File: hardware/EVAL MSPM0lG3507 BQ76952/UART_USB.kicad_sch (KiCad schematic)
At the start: 14 parts, among them J16 USB_B_Micro, Q1 2N7002, U1 ISO7721D, U12 FT230XS, U4 ISO7721D, U8 TPD4E05U06DQA

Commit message: boards finalized
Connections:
- net GND: now also J16.5 (GND), Q1.3 (D); no longer C8.2, C9.2, Q1.2 (S), U1.4 (GND1), U12.13 (GND), U12.5 (GND), U4.4 (GND1)
- new net: C8.2, C9.2, Q1.2 (S), U1.4 (GND1), U12.13 (GND), U12.5 (GND), U4.4 (GND1)
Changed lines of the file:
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@@
+	(wire
+		(pts
+			(xy 148.59 115.57) (xy 148.59 93.98)
+		)
+		(stroke
+			(width 0)
+			(type default)
+		)
+	)
+	(wire
+		(pts
+			(xy 151.13 86.36) (xy 153.67 86.36)
+		)
+		(stroke
+			(width 0)
+			(type default)
+		)
+	)
+	(wire
+		(pts
+			(xy 115.57 120.65) (xy 115.57 123.19)
+		)
+		(stroke
+			(width 0)
+			(type default)
+		)
+	)
+	(wire
+		(pts
+			(xy 143.51 91.44) (xy 143.51 95.25)
+		)
+		(stroke
+			(width 0)
+			(type default)
+		)
+	)
+	(wire
+		(pts
+			(xy 63.5 102.87) (xy 58.42 102.87)
+		)
+		(stroke
+			(width 0)
+			(type default)
+		)
+	)
+	(wire
+		(pts
+			(xy 50.8 110.49) (xy 50.8 123.19)
+		)
+		(stroke
+			(width 0)
+			(type default)
+		)
+	)
+	(wire
+		(pts
+			(xy 184.15 115.57) (xy 191.77 115.57)
+		)
+		(stroke
+			(width 0)
+			(type default)
+		)
+	)
+	(wire
+		(pts
+			(xy 58.42 100.33) (xy 64.77 100.33)
+		)
+		(stroke
+			(width 0)
+			(type default)
+		)
+	)
+	(wire
+		(pts
+			(xy 135.89 95.25) (xy 143.51 95.25)
+		)
+		(stroke
+			(width 0)
+			(type default)
+		)
+	)
+	(wire
+		(pts
+			(xy 140.97 88.9) (xy 153.67 88.9)
+		)
+		(stroke
+			(width 0)
+			(type default)
+		)
+	)
+	(wire
+		(pts
+			(xy 151.13 107.95) (xy 151.13 86.36)
+		)
+		(stroke
+			(width 0)
+			(type default)
+		)
+	)
+	(polyline
+		(pts
+			(xy 131.572 118.11) (xy 131.572 119.126)
+		)
+		(stroke
+			(width 0)
+			(type default)
+			(color 218 0 255 1)
+		)
+	)
+	(wire
+		(pts
+			(xy 120.65 81.28) (xy 88.9 81.28)
+		)
+		(stroke
+			(width 0)
+			(type default)
+		)
+	)
+	(wire
+		(pts
+			(xy 92.71 92.71) (xy 100.33 92.71)
+		)
+		(stroke
+			(width 0)
+			(type default)
+		)
+	)
+	(wire
+		(pts
+			(xy 135.89 97.79) (xy 143.51 97.79)
+		)
+		(stroke
+			(width 0)
+			(type default)
+		)
+	)
 	(wire
 		(pts
 			(xy 71.12 123.19) (xy 76.2 123.19)
-		)
-		(stroke
-			(width 0)
-			(type default)
-		)
-	)
-	(wire
-		(pts
-			(xy 148.59 115.57) (xy 148.59 93.98)
-		)
-		(stroke
-			(width 0)
-			(type default)
-		)
-	)
-	(wire
-		(pts
-			(xy 151.13 86.36) (xy 153.67 86.36)
-		)
-		(stroke
-			(width 0)
-			(type default)
-		)
-	)
-	(wire
-		(pts
-			(xy 115.57 120.65) (xy 115.57 123.19)
-		)
-		(stroke
-			(width 0)
-			(type default)
-		)
-	)
-	(wire
-		(pts
-			(xy 143.51 91.44) (xy 143.51 95.25)
-		)
-		(stroke
-			(width 0)
-			(type default)
-		)
-	)
-	(wire
-		(pts
-			(xy 63.5 102.87) (xy 58.42 102.87)
-		)
-		(stroke
-			(width 0)
-			(type default)
-		)
-	)
-	(wire
-		(pts
-			(xy 50.8 110.49) (xy 50.8 123.19)
-		)
-		(stroke
-			(width 0)
-			(type default)
-		)
-	)
-	(wire
-		(pts
-			(xy 184.15 115.57) (xy 191.77 115.57)
-		)
-		(stroke
-			(width 0)
-			(type default)
-		)
-	)
-	(wire
-		(pts
-			(xy 58.42 100.33) (xy 64.77 100.33)
-		)
-		(stroke
-			(width 0)
-			(type default)
-		)
-	)
-	(wire
-		(pts
-			(xy 135.89 95.25) (xy 143.51 95.25)
-		)
-		(stroke
-			(width 0)
-			(type default)
-		)
-	)
-	(wire
-		(pts
-			(xy 140.97 88.9) (xy 153.67 88.9)
-		)
-		(stroke
-			(width 0)
-			(type default)
-		)
-	)
-	(wire
-		(pts
-			(xy 151.13 107.95) (xy 151.13 86.36)
-		)
-		(stroke
-			(width 0)
-			(type default)
-		)
-	)
-	(polyline
-		(pts
-			(xy 131.572 118.11) (xy 131.572 119.126)
-		)
-		(stroke
-			(width 0)
-			(type default)
-			(color 218 0 255 1)
-		)
-	)
-	(wire
-		(pts
-			(xy 120.65 81.28) (xy 88.9 81.28)
-		)
-		(stroke
-			(width 0)
-			(type default)
-		)
-	)
-	(wire
-		(pts
-			(xy 92.71 92.71) (xy 100.33 92.71)
-		)
-		(stroke
-			(width 0)
-			(type default)
-		)
-	)
-	(wire
-		(pts
-			(xy 135.89 97.79) (xy 143.51 97.79)
 		)
 		(stroke
@@
 	)
 	(label "GND"
-		(at 101.6 123.19 0)
+		(at 54.61 123.19 0)
 		(effects
 			(font

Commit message: partial correctinos to kicad
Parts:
- removed Q1: 2N7002, Package_TO_SOT_SMD:SOT-23, symbol Transistor_FET:2N7002
- removed R49: 4.99k, Resistor_SMD:R_1206_3216Metric_Pad1.30x1.75mm_HandSolder, symbol Device:R_US
- removed TP19: TestPoint, TestPoint:TestPoint_Loop_D2.50mm_Drill1.0mm_LowProfile, symbol Connector:TestPoint
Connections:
- net GND: now also C8.2, C9.2, U1.4 (GND1), U12.13 (GND), U12.5 (GND), U4.4 (GND1)
- net VBUS_5v: no longer C8.1, J16.1 (VBUS), U12.12 (VCC)
- new net: C8.1, J16.1 (VBUS), U12.12 (VCC)
- no-connect marks 12 -> 13
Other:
- note added: "ground if is host. floating if is peripheral"
- note removed: "ground if u r host. floating if u r peripheral"

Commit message: asdd
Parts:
- removed C8: 220n, Capacitor_SMD:C_1206_3216Metric_Pad1.33x1.80mm_HandSolder, symbol Device:C_Small
- removed TP20, TP29, TP30, TP31: TestPoint, TestPoint:TestPoint_Loop_D2.50mm_Drill1.0mm_LowProfile, symbol Connector:TestPoint
- added C18, C8: 33uF, Diode_SMD:D_1206_3216Metric_Pad1.42x1.75mm_HandSolder, symbol Device:C_Polarized_Small_US
- added C19, C20: 220n, Capacitor_SMD:C_1206_3216Metric_Pad1.33x1.80mm_HandSolder, symbol Device:C_Small
- added JP2, JP3: SolderJumper_2_Open, Jumper:SolderJumper-2_P1.3mm_Open_TrianglePad1.0x1.5mm, symbol Jumper:SolderJumper_2_Open
- added U3: LM3940IMP-3.3/NOPB, Package_TO_SOT_SMD:SOT-223-3_TabPin2, symbol zzLocalLibrary:LM3904imp-3.3/NOPB
- U8: now not fitted; now left out of the parts list
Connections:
- net D+: no longer J16.3 (D+), U12.8 (USBDP)
- net D-: no longer J16.2 (D-), U12.9 (USBDM)
- net GND: now also C18.2, C19.2, C20.2, C8.2, U3.2 (GND)
- net at C9.1, U1.1 (VCC1), U12.3 (VCCIO)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: now also JP2.1 (A), JP3.2 (B); no longer U12.10 (3V3OUT)
- net at J16.1 (VBUS): now also C19.1, C20.1, U3.1 (5v_IN); no longer U12.12 (VCC)
- new net: J16.2 (D-), U12.9 (USBDM)
- new net: J16.3 (D+), U12.8 (USBDP)
- new net: C18.1, C8.1, JP2.2 (B), U12.12 (VCC), U3.3 (3v3_OUT)
- new net: JP3.1 (A), U12.10 (3V3OUT)
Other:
- note added: "cap config: ds.8.2"
- note added: "datasheet uses strange wording, if broke try jumping these"
- note removed: "ground if is host. floating if is peripheral"
- moved on the sheet: J16

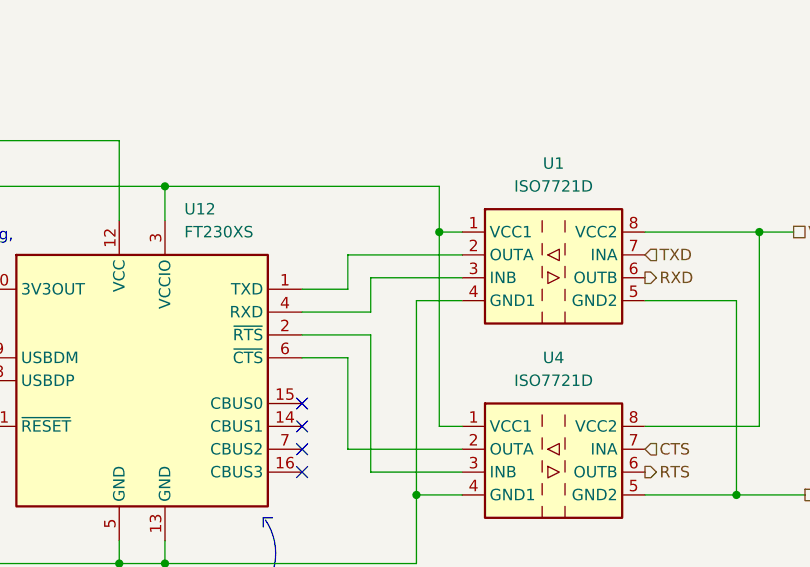
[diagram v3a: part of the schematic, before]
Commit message: updtates
Fixed George's mistake of input/output pins.

Co-Authored-By: Manish Shrestha <manish.shr006@gmail.com>
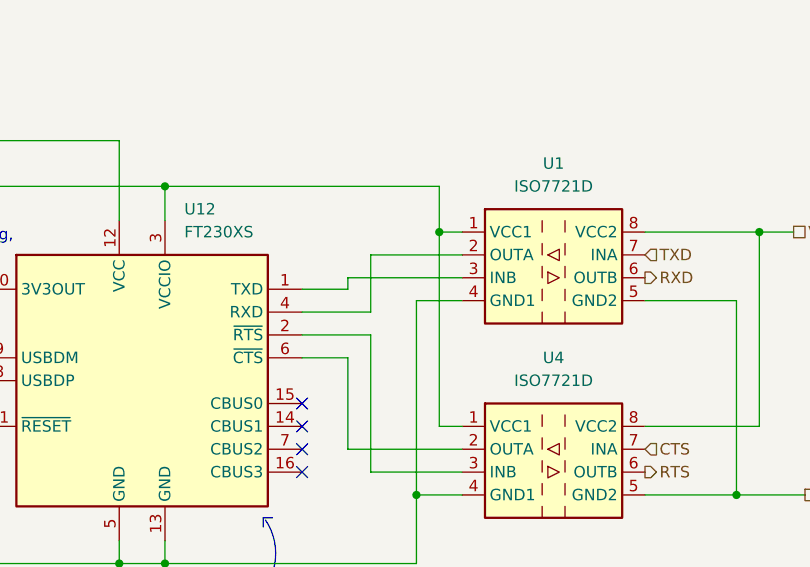
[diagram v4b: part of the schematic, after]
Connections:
- net at U1.2 (OUTA): now also U12.4 (RXD); no longer U12.1 (TXD)
- net at U1.3 (INB): now also U12.1 (TXD); no longer U12.4 (RXD)
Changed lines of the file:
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@@
-	(wire
-		(pts
-			(xy 140.97 92.71) (xy 140.97 88.9)
-		)
-		(stroke
-			(width 0)
-			(type default)
-		)
-	)
 	(wire
 		(pts
@@
 	(wire
 		(pts
-			(xy 153.67 91.44) (xy 143.51 91.44)
-		)
-		(stroke
-			(width 0)
-			(type default)
-		)
-	)
-	(wire
-		(pts
 			(xy 143.51 97.79) (xy 143.51 113.03)
 		)
@@
 	(wire
 		(pts
+			(xy 140.97 92.71) (xy 140.97 91.44)
+		)
+		(stroke
+			(width 0)
+			(type default)
+		)
+	)
+	(wire
+		(pts
 			(xy 186.69 86.36) (xy 186.69 107.95)
 		)
@@
 	(wire
 		(pts
-			(xy 143.51 91.44) (xy 143.51 95.25)
+			(xy 143.51 88.9) (xy 143.51 95.25)
 		)
 		(stroke
@@
 	(wire
 		(pts
-			(xy 140.97 88.9) (xy 153.67 88.9)
-		)
-		(stroke
-			(width 0)
-			(type default)
-		)
-	)
-	(wire
-		(pts
 			(xy 151.13 107.95) (xy 151.13 86.36)
 		)
@@
 	(wire
 		(pts
+			(xy 143.51 88.9) (xy 153.67 88.9)
+		)
+		(stroke
+			(width 0)
+			(type default)
+		)
+	)
+	(wire
+		(pts
 			(xy 88.9 81.28) (xy 88.9 92.71)
 		)
@@
 		)
 		(stroke
+			(width 0)
+			(type default)
+		)
+	)
+	(wire
+		(pts
+			(xy 140.97 91.44) (xy 153.67 91.44)
+		)
+		(stroke

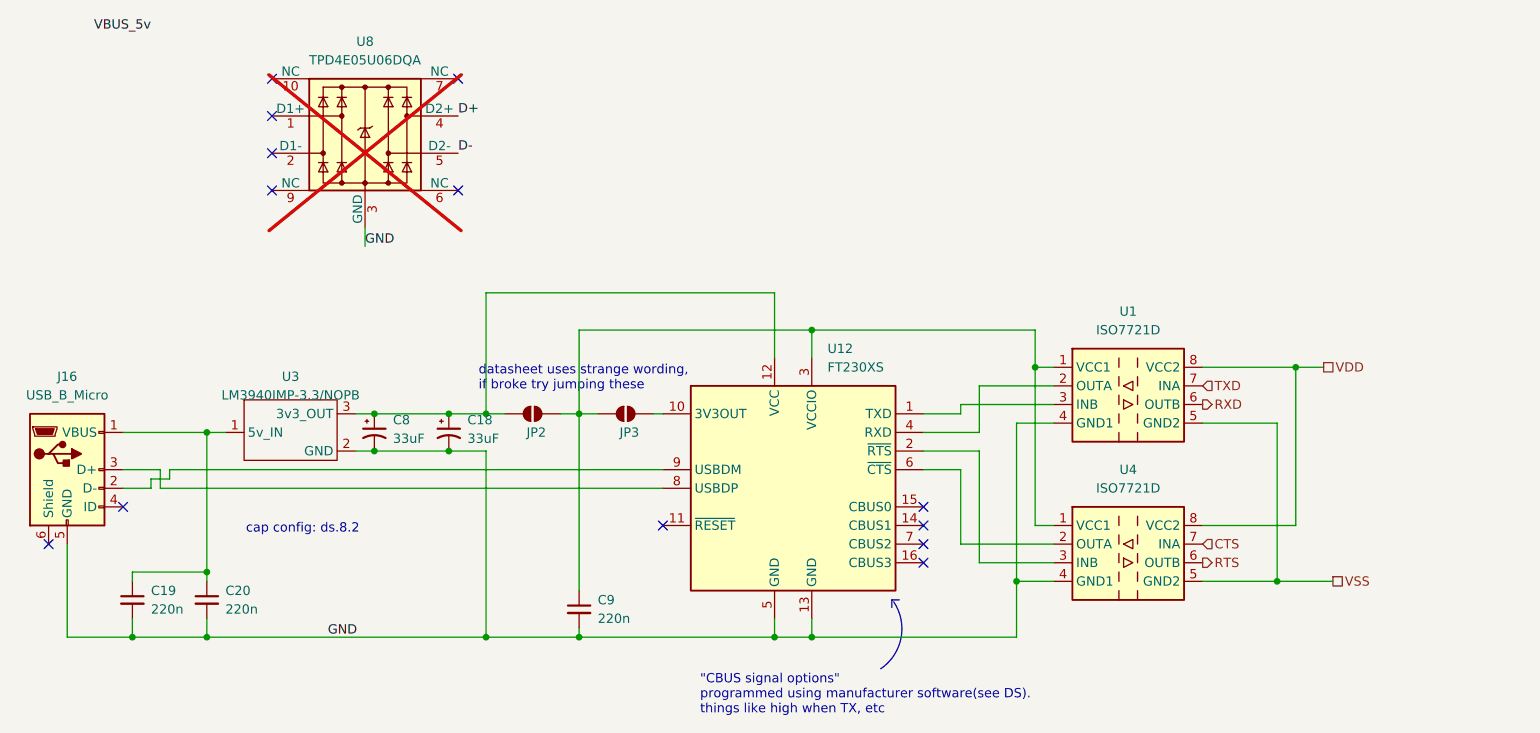
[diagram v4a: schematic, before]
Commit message: corrected CAN transceiver parts
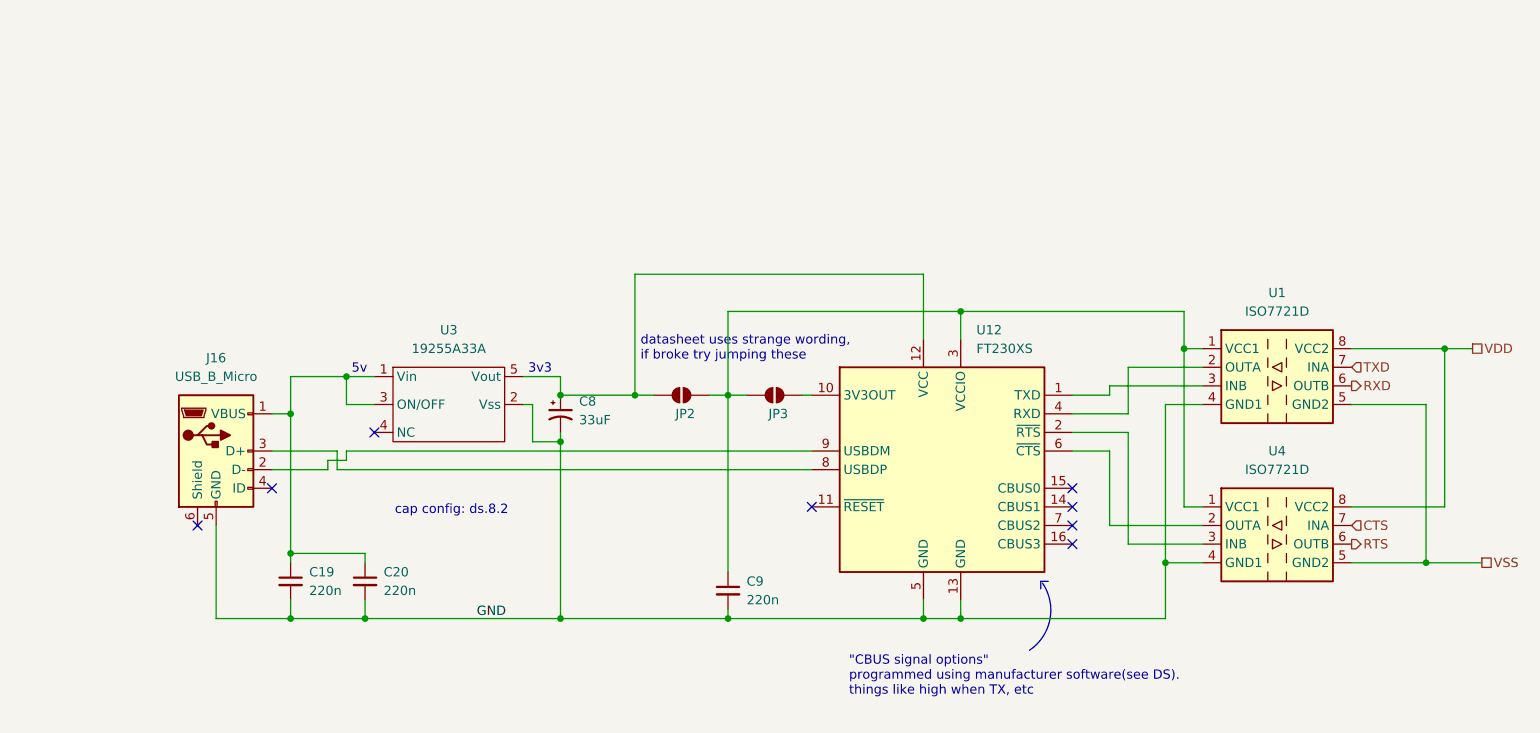
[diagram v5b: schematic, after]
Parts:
- removed C18: 33uF, Diode_SMD:D_1206_3216Metric_Pad1.42x1.75mm_HandSolder, symbol Device:C_Polarized_Small_US
- removed U3: LM3940IMP-3.3/NOPB, Package_TO_SOT_SMD:SOT-223-3_TabPin2, symbol zzLocalLibrary:LM3904imp-3.3/NOPB
- removed U8: TPD4E05U06DQA, Package_SON:USON-10_2.5x1.0mm_P0.5mm, symbol Power_Protection:TPD4E05U06DQA
- added U3: 19255A33A, Package_TO_SOT_SMD:SOT-23-5_HandSoldering, symbol zzLocalLibrary:S-19255A33A-M5T1U4
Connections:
- net GND: now also U3.2 (Vss)
- net at C19.1, C20.1, J16.1 (VBUS): now also U3.1 (Vin), U3.3 (ON/OFF)
- net at C8.1, JP2.2 (B), U12.12 (VCC): now also U3.5 (Vout)
- no-connect marks 13 -> 8
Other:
- note added: "3v3"
- note added: "5v"
- moved on the sheet: C19, C20, C8, C9, J16, JP2, JP3, U1, U12, U4

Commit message: bluhhh
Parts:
- removed C8: 33uF, Diode_SMD:D_1206_3216Metric_Pad1.42x1.75mm_HandSolder, symbol Device:C_Polarized_Small_US
- added C24, C8: 10u, Capacitor_SMD:C_1206_3216Metric_Pad1.33x1.80mm_HandSolder, symbol Device:C_Small
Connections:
- net GND: now also C24.2, C8.2
- net at JP2.2 (B), U12.12 (VCC), U3.5 (Vout): now also C24.1, C8.1
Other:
- moved on the sheet: U3

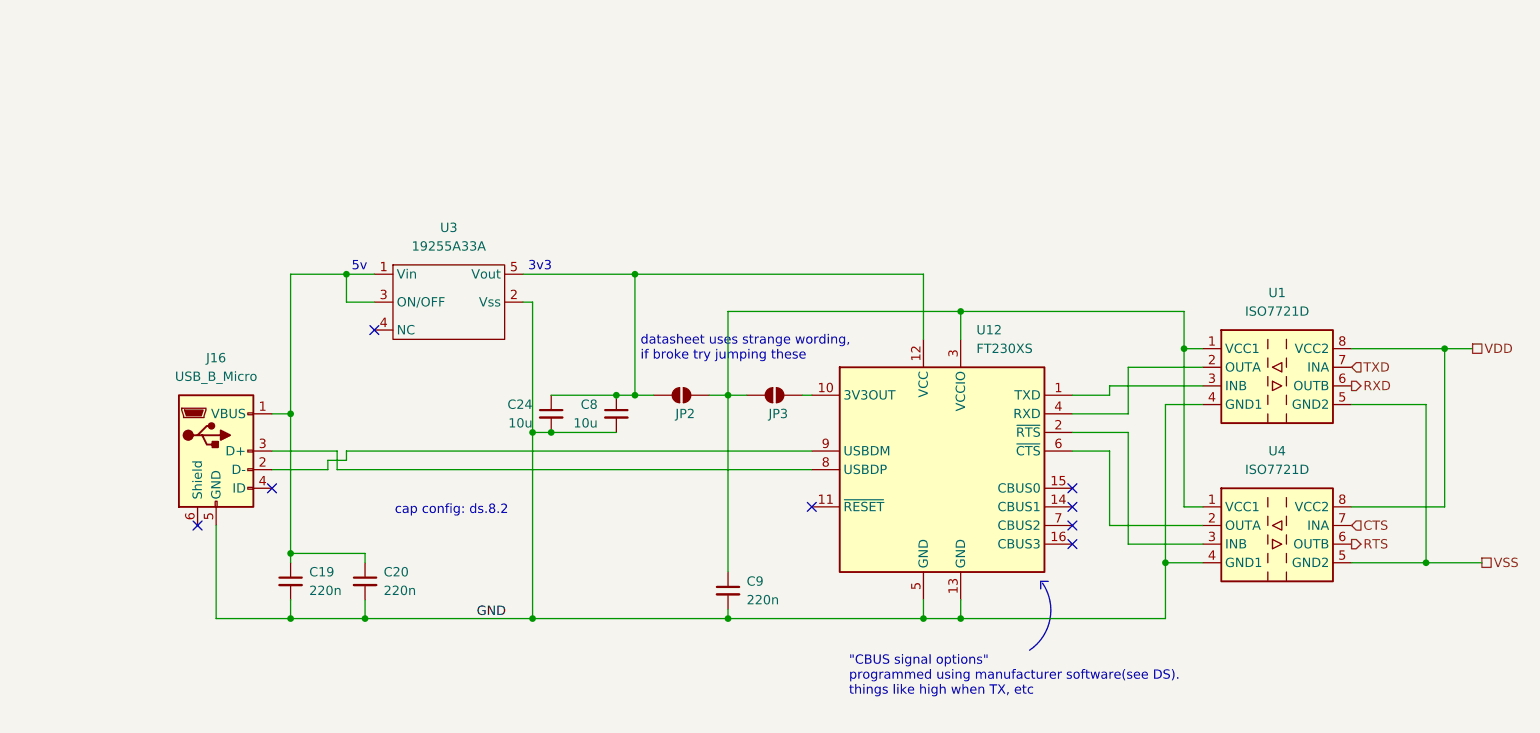
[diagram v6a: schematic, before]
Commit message: better regulator for usb
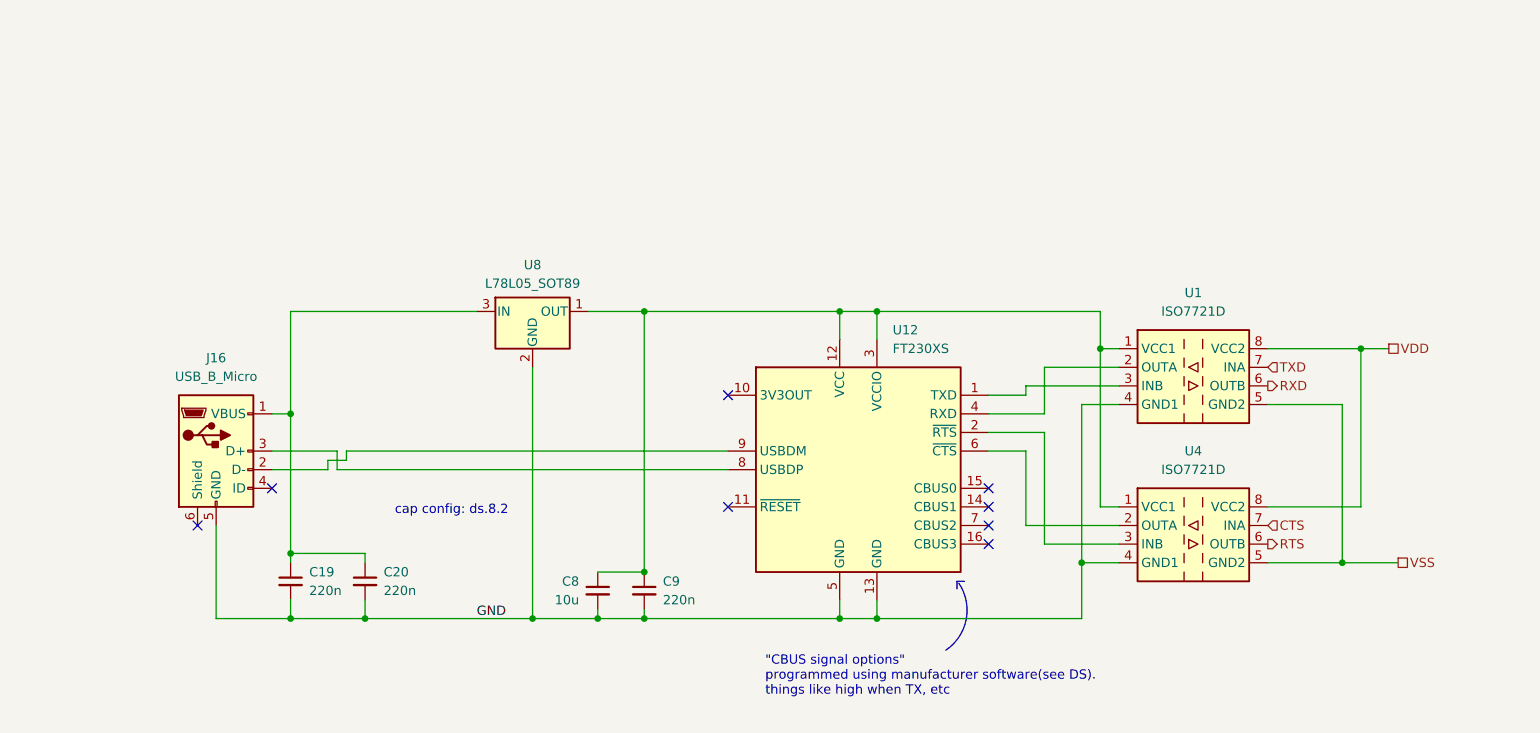
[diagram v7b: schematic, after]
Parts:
- removed C24: 10u, Capacitor_SMD:C_1206_3216Metric_Pad1.33x1.80mm_HandSolder, symbol Device:C_Small
- removed JP2, JP3: SolderJumper_2_Open, Jumper:SolderJumper-2_P1.3mm_Open_TrianglePad1.0x1.5mm, symbol Jumper:SolderJumper_2_Open
- removed U3: 19255A33A, Package_TO_SOT_SMD:SOT-23-5_HandSoldering, symbol zzLocalLibrary:S-19255A33A-M5T1U4
- added U8: L78L05_SOT89, Package_TO_SOT_SMD:SOT-89-3, symbol Regulator_Linear:L78L05_SOT89
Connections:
- net GND: now also U8.2 (GND)
- net at C9.1, U1.1 (VCC1), U12.3 (VCCIO)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: now also C8.1, U12.12 (VCC), U8.1 (OUT)
- net at C19.1, C20.1, J16.1 (VBUS): now also U8.3 (IN)
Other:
- note removed: "3v3"
- note removed: "5v"
- note removed: "datasheet uses strange wording, if broke try jumping these"
- moved on the sheet: C8, C9, U1, U12, U4

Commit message: ac;lkacnl;
acea;kca
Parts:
- removed C8: 10u, Capacitor_SMD:C_1206_3216Metric_Pad1.33x1.80mm_HandSolder, symbol Device:C_Small
- removed C9: 220n, Capacitor_SMD:C_1206_3216Metric_Pad1.33x1.80mm_HandSolder, symbol Device:C_Small
- removed U4: ISO7721D, Package_SO:SOIC-8_3.9x4.9mm_P1.27mm, symbol Isolator:ISO7721D
- removed U8: L78L05_SOT89, Package_TO_SOT_SMD:SOT-89-3, symbol Regulator_Linear:L78L05_SOT89
- added D5: LED, LED_SMD:LED_0603_1608Metric, symbol Device:LED
- added R10: 750, Resistor_SMD:R_1206_3216Metric_Pad1.30x1.75mm_HandSolder, symbol Device:R_US
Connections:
- net at U1.1 (VCC1), U12.12 (VCC), U12.3 (VCCIO): now also C19.1, C20.1, J16.1 (VBUS), R10.1
- net GND: no longer names the net of C19.2, C20.2, J16.5 (GND), U1.4 (GND1), U12.13 (GND), U12.5 (GND)
- net GND: now also D5.1 (K)
- new net: D5.2 (A), R10.2
- no-connect marks 8 -> 10
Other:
- note removed: "cap config: ds.8.2"
- moved on the sheet: U1, U12
